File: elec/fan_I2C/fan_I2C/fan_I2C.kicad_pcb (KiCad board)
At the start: 2 copper layers, 126.3 x 160 mm, 72 parts, among them J101 DB25_Female_MountingHoles, J102 DB9_Female_MountingHoles, J103 Screw_Terminal_01x02, J104 Conn_01x04, J105 Conn_01x05, J106 Conn_01x04, J107 Conn_01x07, J108 Screw_Terminal_01x02, J109 Conn_02x12_Odd_Even, J201 0.100_2Pin, J202 Conn_01x04, J301 RJ12_6P6C_HORZ, J302 0.100_2Pin, Q201 BSS138, Q202 BSS138, Q301 BSS138, Q302 BSS138, Q303 BSS138, Q304 BSS138, SW101 SW_DIP_x08

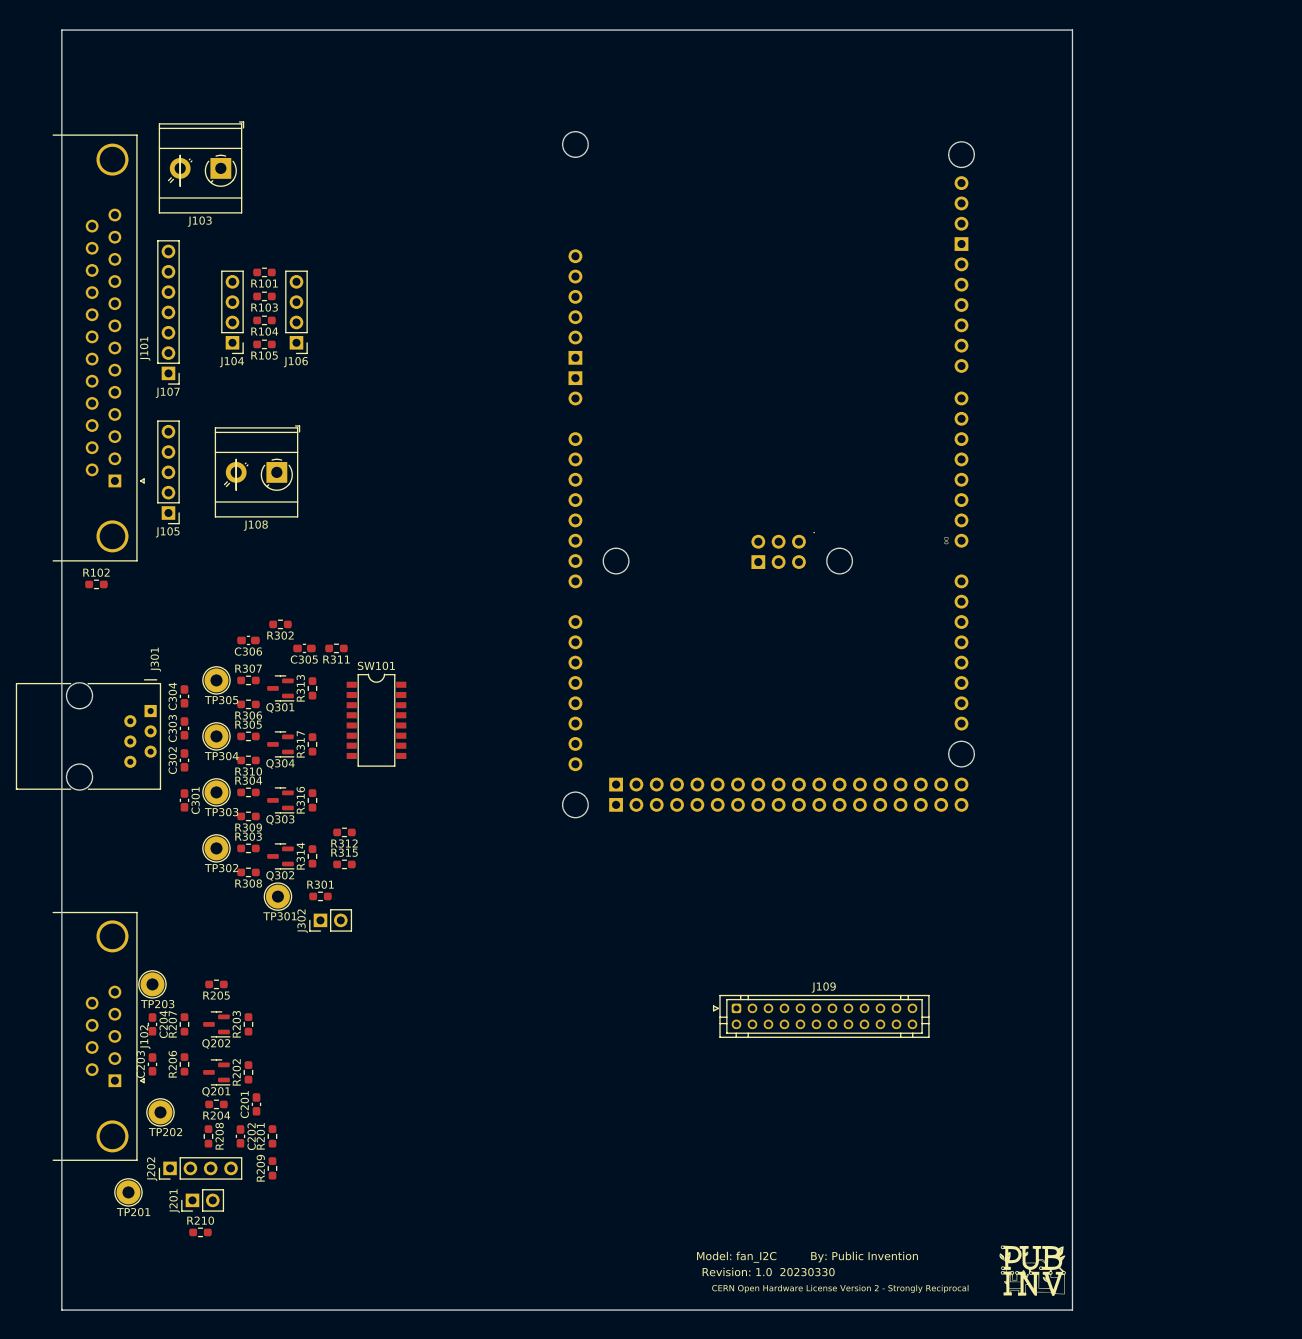
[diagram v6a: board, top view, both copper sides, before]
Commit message: Add mounting holes.
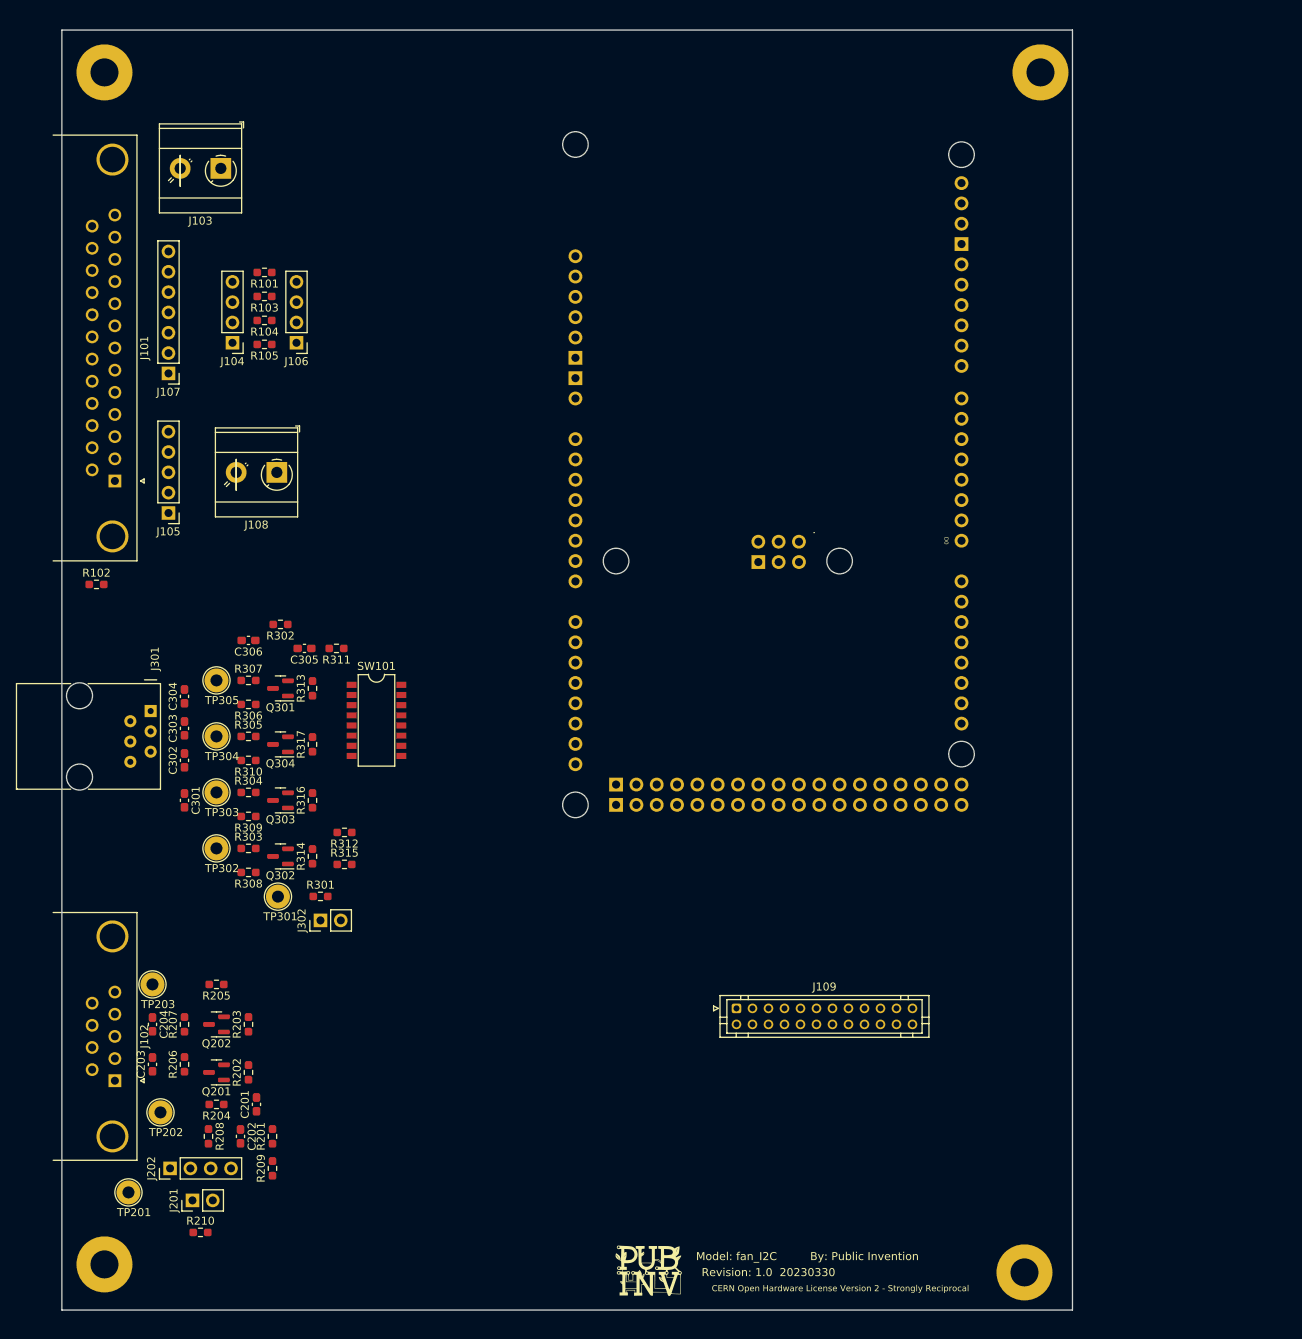
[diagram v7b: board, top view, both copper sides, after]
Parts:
- added ?: , , F.Cu at (39.0, 27.0)
- added ?: , , F.Cu at (39.0, 176.0)
- added ?: , , F.Cu at (156.0, 27.0)
- added ?: , , F.Cu at (154.0, 177.0)
- moved G*** 48.0 mm to (107.0, 177.0)
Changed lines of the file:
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@@
     )
   )
+  (footprint "" (layer "F.Cu")
+    (at 39 27)
+    (fp_text reference "" (at 0 0) (layer "F.SilkS")
+      (effects (font (size 1.27 1.27) (thickness 0.15)))
+    )
+    (fp_text value "" (at 0 0) (layer "F.SilkS")
+      (effects (font (size 1.27 1.27) (thickness 0.15)))
+    )
+    (pad "1" thru_hole circle locked (at 0 0) (size 7 7) (drill 3.5) (layers *.Cu *.Mask)
+      (net 1 "GND") (pinfunction "1") (pintype "input"))
+  )
   (footprint "Capacitor_SMD:C_0603_1608Metric_Pad1.08x0.95mm_HandSolder" (layer "F.Cu")
     (at 56 160 -90)
@@
   )
   (footprint "PubInv_PCB:Logo_PI_BandW_70percent_10x10" (layer "F.Cu")
-    (at 155 177)
+    (at 107 177)
     (attr board_only exclude_from_pos_files exclude_from_bom)
     (fp_text reference "G***" (at 0.262786 5.08) (layer "F.SilkS") hide
@@
     (fp_arc (start 88.138 -53.594) (mid 90.17 -54.254237) (end 92.202 -53.594) (layer "B.CrtYd") (width 0.15))
     (fp_arc (start 98.552 0.254) (mid 96.52 0.914237) (end 94.488 0.254) (layer "B.CrtYd") (width 0.15))
-    (fp_arc (start 99.8728 -1.7018) (mid 99.650928 -1.077972) (end 99.314 -0.508) (layer "B.CrtYd") (width 0.15))
+    (fp_arc (start 99.8728 -1.7018) (mid 99.650934 -1.077968) (end 99.314 -0.508) (layer "B.CrtYd") (width 0.15))
     (fp_arc (start 13.208 -53.594) (mid 15.24 -54.254237) (end 17.272 -53.594) (layer "B.CrtYd") (width 0.15))
     (fp_circle (center 13.97 -2.54) (end 17.42 -2.54) (layer "F.CrtYd") (width 0.15) (fill none))
@@
     )
   )
+  (footprint "" (layer "F.Cu")
+    (at 39 176)
+    (fp_text reference "" (at 0 0) (layer "F.SilkS")
+      (effects (font (size 1.27 1.27) (thickness 0.15)))
+    )
+    (fp_text value "" (at 0 0) (layer "F.SilkS")
+      (effects (font (size 1.27 1.27) (thickness 0.15)))
+    )
+    (pad "1" thru_hole circle locked (at 0 0) (size 7 7) (drill 3.5) (layers *.Cu *.Mask)
+      (net 1 "GND") (pinfunction "1") (pintype "input"))
+  )
   (footprint "TestPoint:TestPoint_Loop_D2.54mm_Drill1.5mm_Beaded" (layer "F.Cu")
     (at 60.684237 130.026)
@@
     )
   )
+  (footprint "" (layer "F.Cu")
+    (at 156 27)
+    (fp_text reference "" (at 0 0) (layer "F.SilkS")
+      (effects (font (size 1.27 1.27) (thickness 0.15)))
+    )
+    (fp_text value "" (at 0 0) (layer "F.SilkS")
+      (effects (font (size 1.27 1.27) (thickness 0.15)))
+    )
+    (pad "1" thru_hole circle locked (at 0 0) (size 7 7) (drill 3.5) (layers *.Cu *.Mask)
+      (net 1 "GND") (pinfunction "1") (pintype "input"))
+  )
   (footprint "Connector_Dsub:DSUB-25_Female_Horizontal_P2.77x2.84mm_EdgePinOffset4.94mm_Housed_MountingHolesOffset7.48mm" locked (layer "F.Cu")
     (at 40.3 78.07 -90)
@@
     )
   )
+  (footprint "" (layer "F.Cu")
+    (at 154 177)
+    (fp_text reference "" (at 0 0) (layer "F.SilkS")
+      (effects (font (size 1.27 1.27) (thickness 0.15)))
+    )
+    (fp_text value "" (at 0 0) (layer "F.SilkS")
+      (effects (font (size 1.27 1.27) (thickness 0.15)))
+    )
+    (pad "1" thru_hole circle locked (at 0 0) (size 7 7) (drill 3.5) (layers *.Cu *.Mask)
+      (net 1 "GND") (pinfunction "1") (pintype "input"))
+  )
   (footprint "Resistor_SMD:R_0603_1608Metric_Pad0.98x0.95mm_HandSolder" (layer "F.Cu")

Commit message: Add 3D model to Arduino.
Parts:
- XA101: footprint arduino-library:Arduino_Due_Shield -> PubInv_PCB:Arduino_Due_Shield
